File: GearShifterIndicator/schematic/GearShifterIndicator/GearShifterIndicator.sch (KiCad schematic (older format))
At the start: 1 part

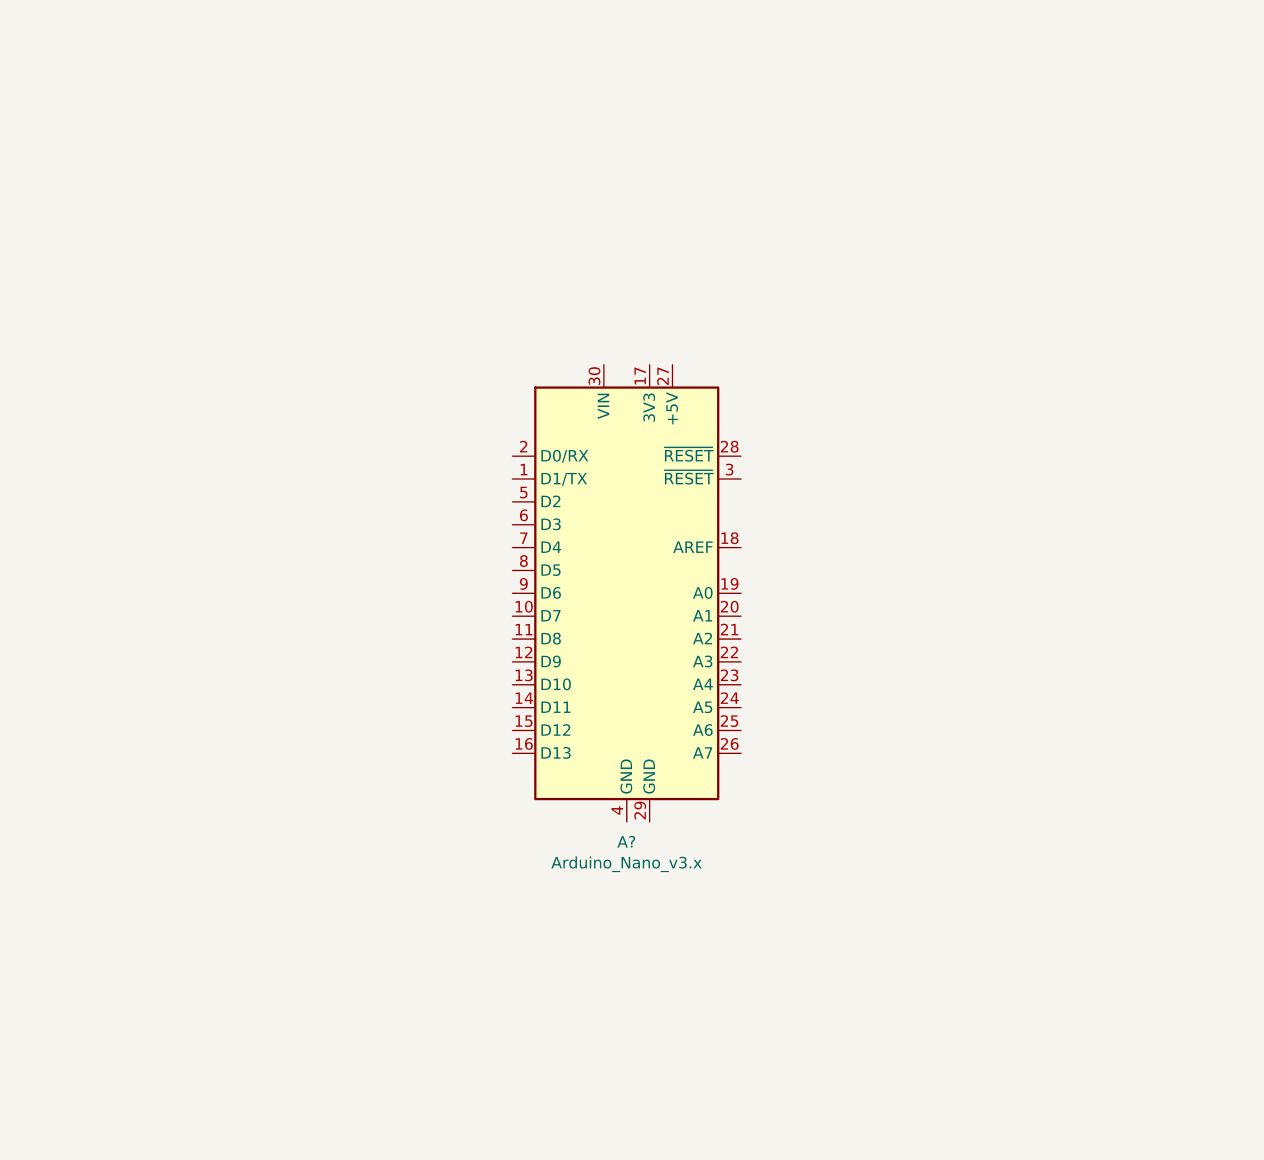
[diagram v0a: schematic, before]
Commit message: Started
Added a PinChangeInterrupt Library, but may take out due to the many errors
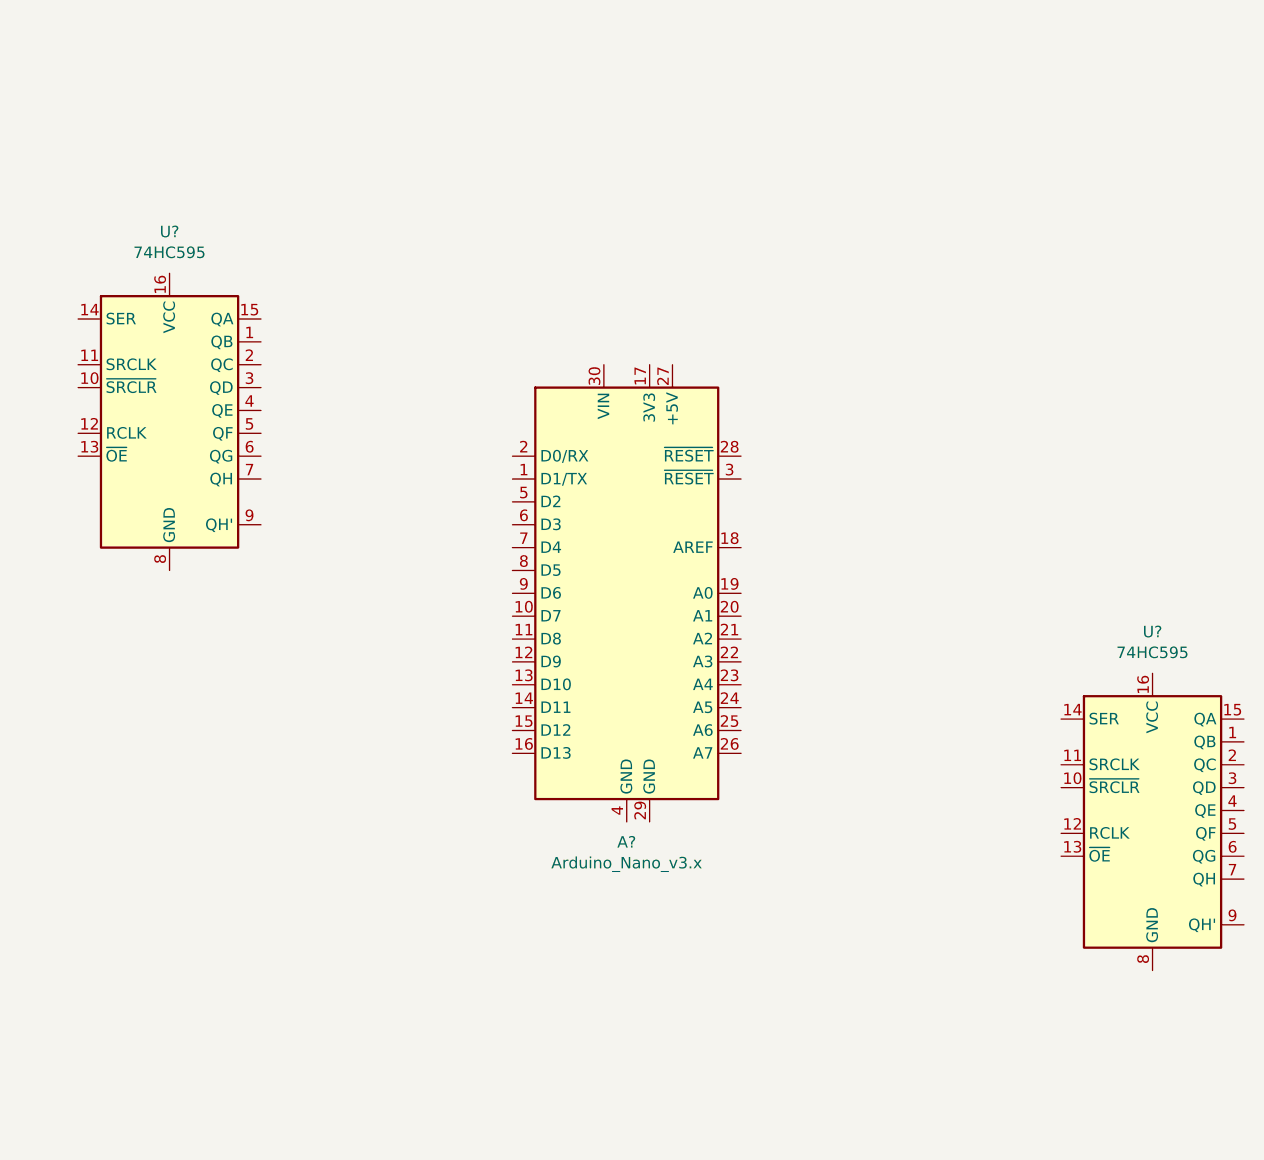
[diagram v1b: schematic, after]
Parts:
- added U? (x2): 74HC595, symbol 74xx:74HC595
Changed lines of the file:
@@
+	1    0    0    -1
+$EndComp
+$Comp
+L 74xx:74HC595 U?
+U 1 1 60AF4EE7
+P 3800 2800
+F 0 "U?" H 3800 3581 50  0000 C CNN
+F 1 "74HC595" H 3800 3490 50  0000 C CNN
+F 2 "" H 3800 2800 50  0001 C CNN
+F 3 "http://www.ti.com/lit/ds/symlink/sn74hc595.pdf" H 3800 2800 50  0001 C CNN
+	1    3800 2800
+	1    0    0    -1
+$EndComp
+$Comp
+L 74xx:74HC595 U?
+U 1 1 60AF6663
+P 8100 4550
+F 0 "U?" H 8100 5331 50  0000 C CNN
+F 1 "74HC595" H 8100 5240 50  0000 C CNN
+F 2 "" H 8100 4550 50  0001 C CNN
+F 3 "http://www.ti.com/lit/ds/symlink/sn74hc595.pdf" H 8100 4550 50  0001 C CNN
+	1    8100 4550
 	1    0    0    -1
 $EndComp

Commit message: Restart
Added to Schematic. Created a Block for Hall Effect Sensor. Also Added some data sheets for parts
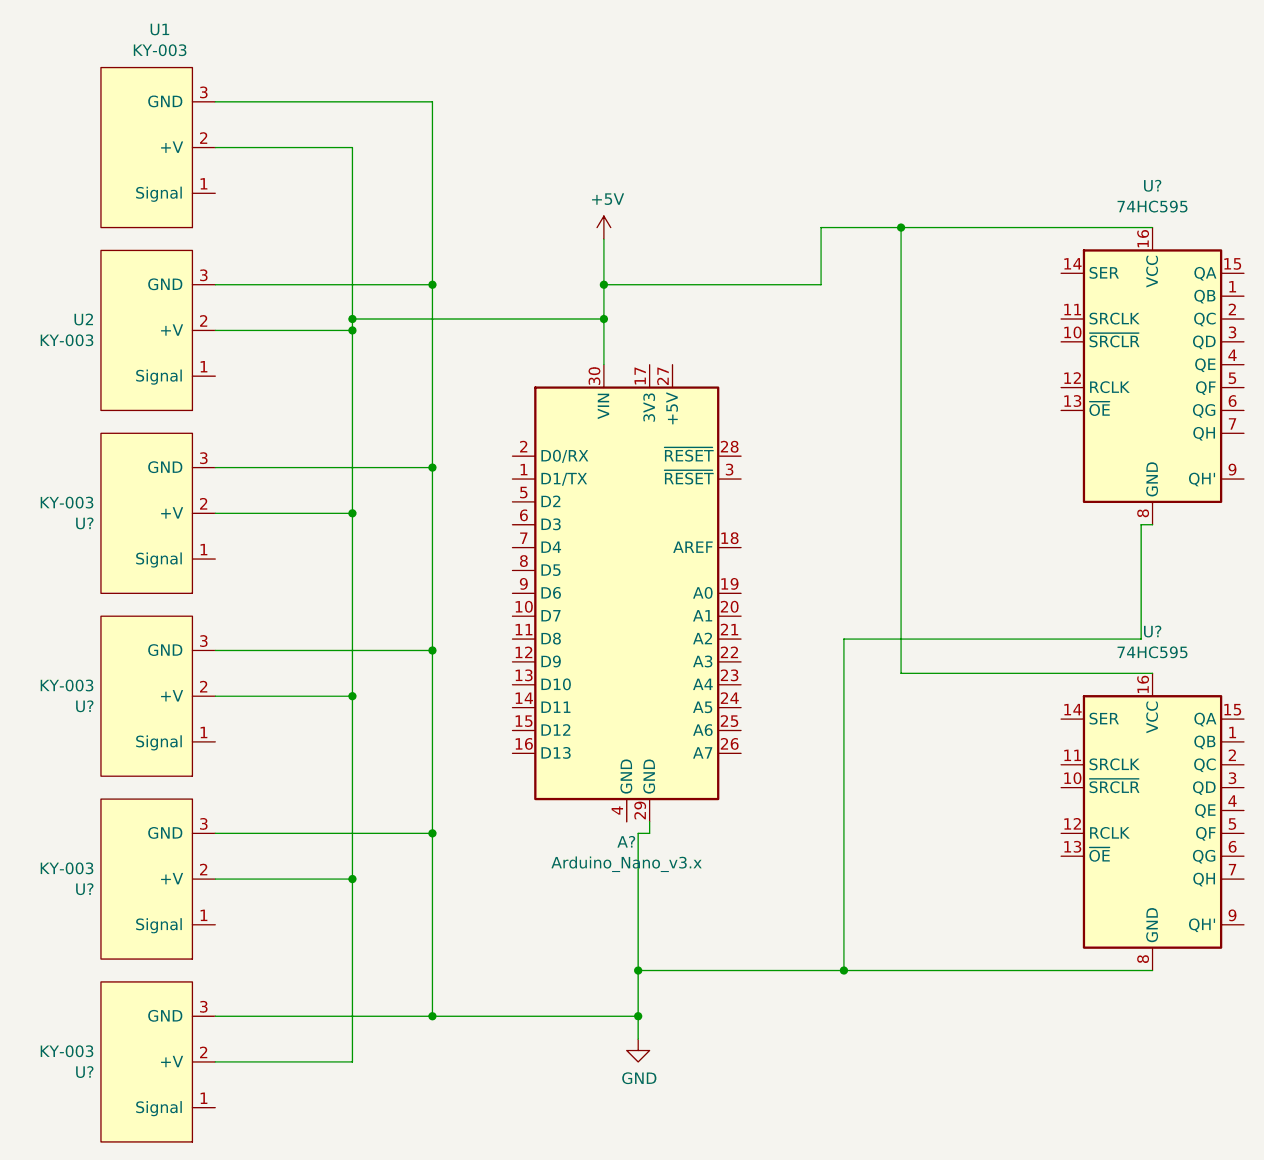
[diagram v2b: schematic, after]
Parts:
- added U1, U2, U? (x4): KY-003, symbol GearShifterIndicator:KY-003
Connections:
- net GND: now reaches A?.29 (GND)
- net GND: now also U?.8 (GND), U?.8 (GND), U1.3 (GND), U2.3 (GND), U?.3 (GND), U?.3 (GND), U?.3 (GND), U?.3 (GND)
- net +5V: now reaches A?.30 (VIN)
- net +5V: now also U?.16 (VCC), U?.16 (VCC), U1.2 (+V), U2.2 (+V), U?.2 (+V), U?.2 (+V), U?.2 (+V), U?.2 (+V)
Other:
- moved on the sheet: U?
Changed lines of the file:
@@
 L 74xx:74HC595 U?
 U 1 1 60AF4EE7
-P 3800 2800
-F 0 "U?" H 3800 3581 50  0000 C CNN
-F 1 "74HC595" H 3800 3490 50  0000 C CNN
-F 2 "" H 3800 2800 50  0001 C CNN
-F 3 "http://www.ti.com/lit/ds/symlink/sn74hc595.pdf" H 3800 2800 50  0001 C CNN
-	1    3800 2800
+P 8100 2600
+F 0 "U?" H 8100 3381 50  0000 C CNN
+F 1 "74HC595" H 8100 3290 50  0000 C CNN
+F 2 "" H 8100 2600 50  0001 C CNN
+F 3 "http://www.ti.com/lit/ds/symlink/sn74hc595.pdf" H 8100 2600 50  0001 C CNN
+	1    8100 2600
 	1    0    0    -1
 $EndComp
@@
 	1    0    0    -1
 $EndComp
+$Comp
+L GearShifterIndicator:KY-003 U2
+U 1 1 6156387F
+P 3700 2450
+F 0 "U2" H 3928 2404 50  0000 L CNN
+F 1 "KY-003" H 3928 2495 50  0000 L CNN
+F 2 "" H 3700 2550 50  0001 C CNN
+F 3 "" H 3700 2550 50  0001 C CNN
+	1    3700 2450
+	-1   0    0    1
+$EndComp
+$Comp
+L GearShifterIndicator:KY-003 U?
+U 1 1 61566826
+P 3700 3250
+F 0 "U?" H 3928 3296 50  0000 L CNN
+F 1 "KY-003" H 3928 3205 50  0000 L CNN
+F 2 "" H 3700 3350 50  0001 C CNN
+F 3 "" H 3700 3350 50  0001 C CNN
+	1    3700 3250
+	-1   0    0    1
+$EndComp
+$Comp
+L GearShifterIndicator:KY-003 U1
+U 1 1 61567877
+P 3700 1650
+F 0 "U1" H 3642 1135 50  0000 C CNN
+F 1 "KY-003" H 3642 1226 50  0000 C CNN
+F 2 "" H 3700 1750 50  0001 C CNN
+F 3 "" H 3700 1750 50  0001 C CNN
+	1    3700 1650
+	-1   0    0    1
+$EndComp
+$Comp
+L GearShifterIndicator:KY-003 U?
+U 1 1 6156C85B
+P 3700 4850
+F 0 "U?" H 3928 4896 50  0000 L CNN
+F 1 "KY-003" H 3928 4805 50  0000 L CNN
+F 2 "" H 3700 4950 50  0001 C CNN
+F 3 "" H 3700 4950 50  0001 C CNN
+	1    3700 4850
+	-1   0    0    1
+$EndComp
+$Comp
+L GearShifterIndicator:KY-003 U?
+U 1 1 6156C865
+P 3700 5650
+F 0 "U?" H 3928 5696 50  0000 L CNN
+F 1 "KY-003" H 3928 5605 50  0000 L CNN
+F 2 "" H 3700 5750 50  0001 C CNN
+F 3 "" H 3700 5750 50  0001 C CNN
+	1    3700 5650
+	-1   0    0    1
+$EndComp
+$Comp
+L GearShifterIndicator:KY-003 U?
+U 1 1 6156C86F
+P 3700 4050
+F 0 "U?" H 3928 4096 50  0000 L CNN
+F 1 "KY-003" H 3928 4005 50  0000 L CNN
+F 2 "" H 3700 4150 50  0001 C CNN
+F 3 "" H 3700 4150 50  0001 C CNN
+	1    3700 4050
+	-1   0    0    1
+$EndComp
+$Comp
+L power:GND #PWR?
+U 1 1 6157D75D
+P 5850 5550
+F 0 "#PWR?" H 5850 5300 50  0001 C CNN
+F 1 "GND" H 5855 5377 50  0000 C CNN
+F 2 "" H 5850 5550 50  0001 C CNN
+F 3 "" H 5850 5550 50  0001 C CNN
+	1    5850 5550
+	1    0    0    -1
+$EndComp
+Wire Wire Line
+	5850 5550 5850 5450
+Wire Wire Line
+	5850 4650 5900 4650
+Wire Wire Line
+	5900 4650 5900 4600
+Wire Wire Line
+	4000 5450 4950 5450
+Wire Wire Line
+	4950 5450 4950 4650
+Wire Wire Line
+	4950 4650 4000 4650
+Wire Wire Line
+	4950 4650 4950 3850
+Wire Wire Line
+	4950 3850 4000 3850
+Connection ~ 4950 4650
+Wire Wire Line
+	4950 3850 4950 3050
+Wire Wire Line
+	4950 3050 4000 3050
+Connection ~ 4950 3850
+Wire Wire Line
+	4950 2250 4000 2250
+Connection ~ 4950 3050
+Wire Wire Line
+	4000 1450 4950 1450
+Wire Wire Line
+	4950 1450 4950 2250
+Connection ~ 4950 2250
+Wire Wire Line
+	4950 2250 4950 3050
+Wire Wire Line
+	4950 5450 5850 5450
+Connection ~ 4950 5450
+Connection ~ 5850 5450
+Wire Wire Line
+	5850 5450 5850 5250
+$Comp
+L power:+5V #PWR?
+U 1 1 61582903
+P 5700 2050
+F 0 "#PWR?" H 5700 1900 50  0001 C CNN
+F 1 "+5V" H 5715 2223 50  0000 C CNN
+F 2 "" H 5700 2050 50  0001 C CNN
+F 3 "" H 5700 2050 50  0001 C CNN
+	1    5700 2050
+	1    0    0    -1
+$EndComp
+Wire Wire Line
+	4000 1650 4600 1650
+Wire Wire Line
+	4600 1650 4600 2400
+Wire Wire Line
+	4600 2450 4000 2450
+Wire Wire Line
+	4600 2450 4600 3250
+Wire Wire Line
+	4600 3250 4000 3250
+Connection ~ 4600 2450
+Wire Wire Line
+	4600 3250 4600 4050
+Wire Wire Line
+	4600 4050 4000 4050
+Connection ~ 4600 3250
+Wire Wire Line
+	4600 4050 4600 4850
+Wire Wire Line
+	4600 4850 4000 4850
+Connection ~ 4600 4050
+Wire Wire Line
+	4000 5650 4600 5650
+Wire Wire Line
+	4600 5650 4600 4850
+Connection ~ 4600 4850
+Wire Wire Line
+	5700 2050 5700 2250
+Wire Wire Line
+	4600 2400 5700 2400
+Connection ~ 4600 2400
+Wire Wire Line
+	4600 2400 4600 2450
+Connection ~ 5700 2400
+Wire Wire Line
+	5700 2400 5700 2600
+Wire Wire Line
+	8050 3300 8050 3800
+Wire Wire Line
+	8050 3800 6750 3800
+Wire Wire Line
+	6750 3800 6750 5250
+Wire Wire Line
+	6750 5250 5850 5250
+Connection ~ 5850 5250
+Wire Wire Line
+	5850 5250 5850 4650
+Wire Wire Line
+	8100 5250 6750 5250
+Connection ~ 6750 5250
+Wire Wire Line
+	6650 2000 6650 2250
+Wire Wire Line
+	6650 2250 5700 2250
+Connection ~ 5700 2250
+Wire Wire Line
+	5700 2250 5700 2400
+Wire Wire Line
+	8100 3950 7000 3950
+Wire Wire Line
+	7000 3950 7000 2000
+Connection ~ 7000 2000
+Wire Wire Line
+	7000 2000 6650 2000
+Wire Wire Line
+	7000 2000 8100 2000
+Wire Wire Line
+	8100 3300 8050 3300
 $EndSCHEMATC
